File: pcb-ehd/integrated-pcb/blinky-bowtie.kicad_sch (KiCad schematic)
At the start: 93 parts, among them J1 USB_C_Receptacle_USB2.0, J2 JST_PH, J3 SWD, Q1 DMP2045U, SW1 B3U, SW2 B3U, SW3 B3U, U1 MCP73831T-2, U2 ATSAMD21G18A-M, U3 AP2112K-3.3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

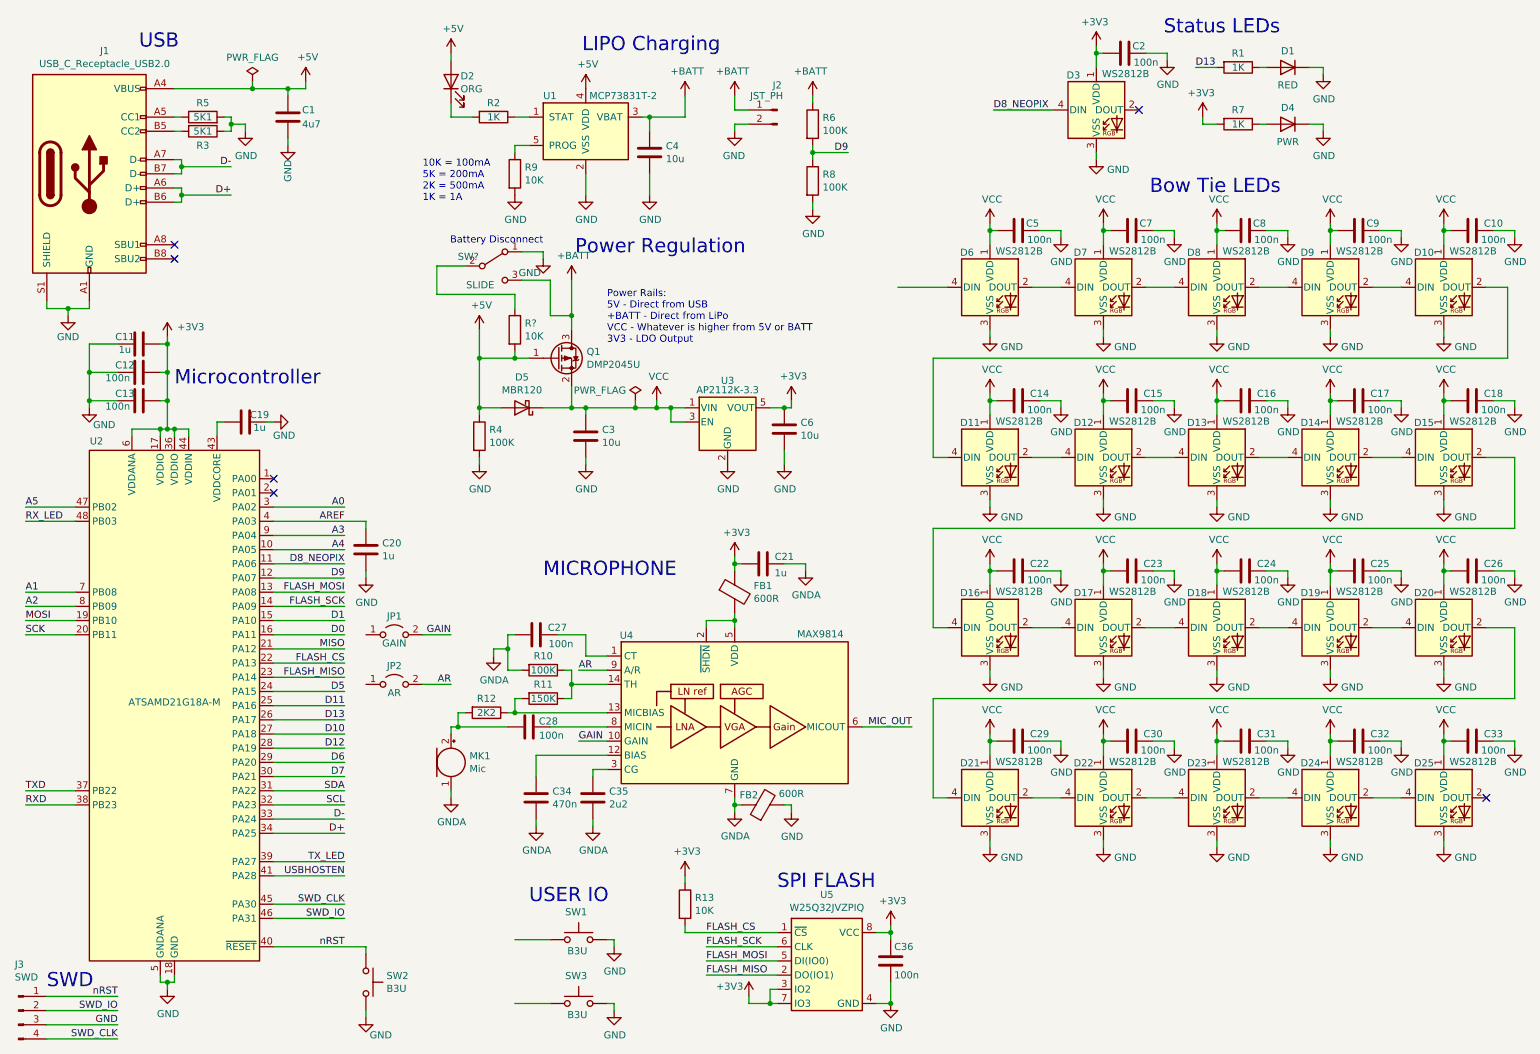
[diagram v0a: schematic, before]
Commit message: bow tie graphics done
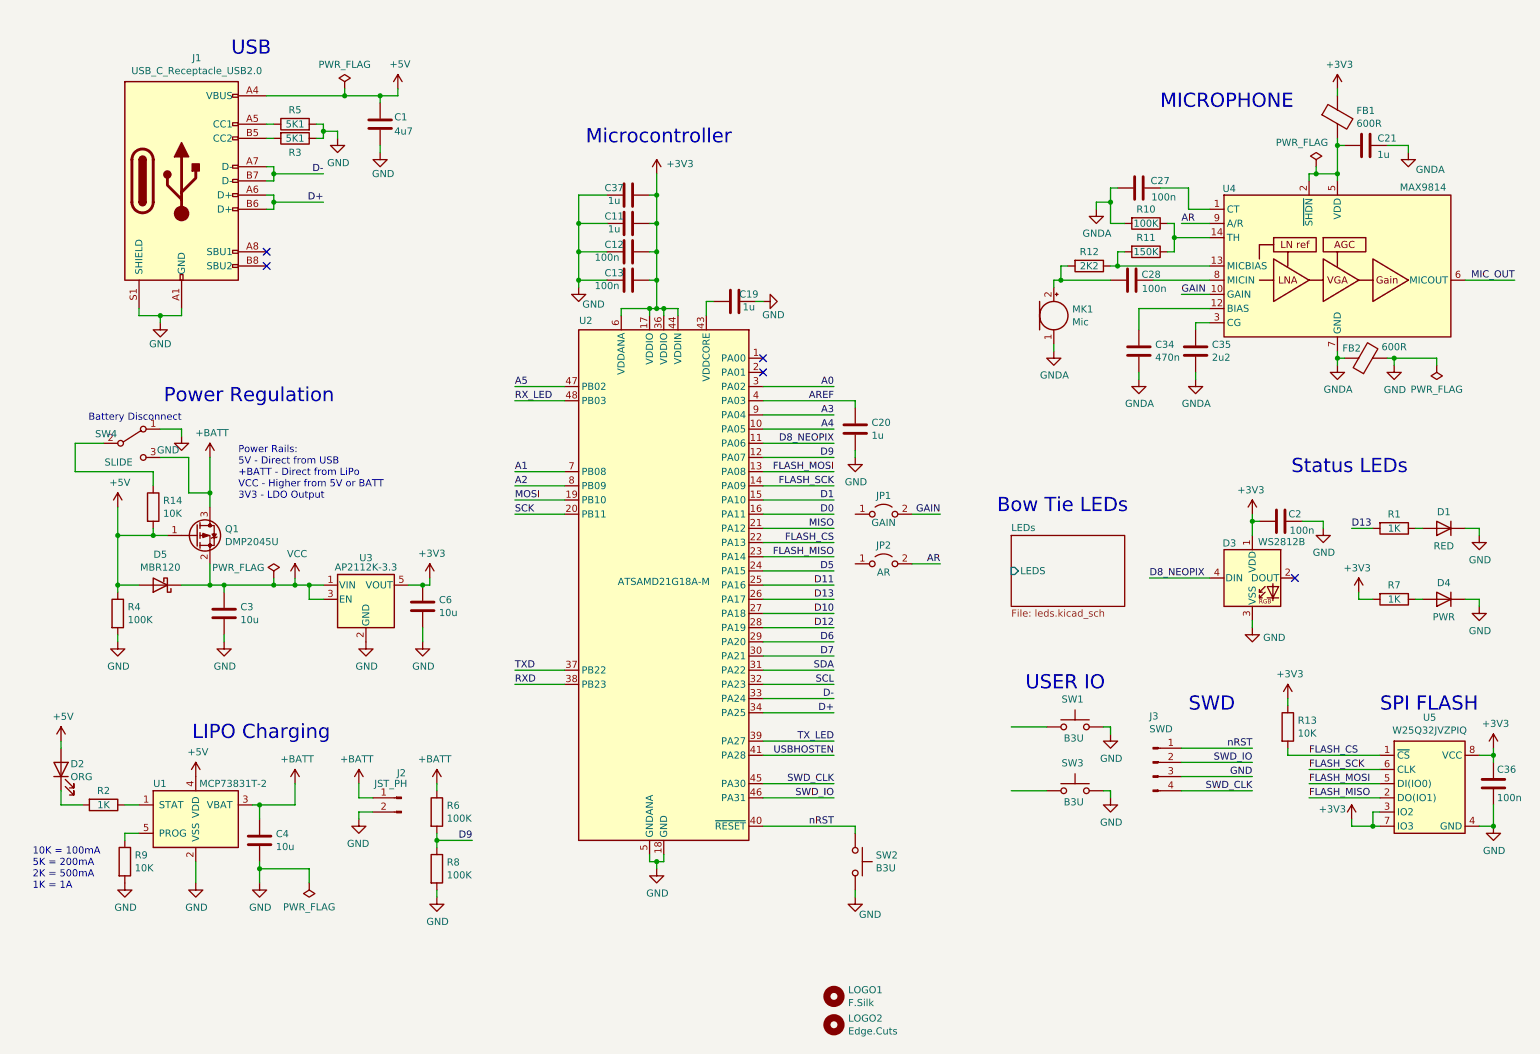
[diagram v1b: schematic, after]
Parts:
- removed C10, C14, C15, C16, C17, C18, C22, C23, C24, C25, C26, C29, C30, C31, C32, C33, C5, C7, C8, C9: 100n, Capacitor_SMD:C_0603_1608Metric, symbol Device:C
- removed D10, D11, D12, D13, D14, D15, D16, D17, D18, D19, D20, D21, D22, D23, D24, D25, D6, D7, D8, D9: WS2812B, LED_SMD:LED_WS2812B_PLCC4_5.0x5.0mm_P3.2mm, symbol LED:WS2812B
- added C37: 1u, Capacitor_SMD:C_0603_1608Metric, symbol Device:C
- added LOGO1: F.Silk, ehd:bowtie-f-silk, symbol Mechanical:MountingHole
- added LOGO2: Edge.Cuts, ehd:bowtie-edge-cuts, symbol Mechanical:MountingHole
- SW4: renamed from SW?; footprint (none) -> ehd:SW_SPDT_PCM12
- gave numbers to parts that had none: 1
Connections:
- net +3V3: now also C37.1; no longer C21.1
- net GND: now also C37.2
- net at FB1.2, U4.2 (~SHDN), U4.5 (VDD): now also C21.1
- no-connect marks 6 -> 5
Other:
- added sheet LEDs (leds.kicad_sch)
- note added: "Power Rails: 5V - Direct from USB +BATT - Direct from LiPo VCC - Higher from 5V or BATT 3V3 - LDO Output"
- note removed: "Power Rails: 5V - Direct from USB +BATT - Direct from LiPo VCC - Whatever is higher from 5V or BATT 3V3 - LDO Output"
- moved on the sheet: C1, C11, C12, C13, C19, C2, C20, C21, C27, C28, C3, C34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

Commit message: rough placement of all but analog
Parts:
- D3: footprint LED_SMD:LED_WS2812B_PLCC4_5.0x5.0mm_P3.2mm -> ehd:LED_WS2812B_PLCC4_5.0x5.0mm_P3.2mm
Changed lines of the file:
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@@
       (effects (font (size 1.27 1.27)) (justify left))
     )
-    (property "Footprint" "LED_SMD:LED_WS2812B_PLCC4_5.0x5.0mm_P3.2mm" (id 2) (at 236.22 121.92 0)
+    (property "Footprint" "ehd:LED_WS2812B_PLCC4_5.0x5.0mm_P3.2mm" (id 2) (at 236.22 121.92 0)
       (effects (font (size 1.27 1.27)) (justify left top) hide)
     )
@@
     )
     (path "/7fb69442-52e3-4c1a-9bf4-99a4ba0d16ef"
-      (reference "D3") (unit 1) (value "WS2812B") (footprint "LED_SMD:LED_WS2812B_PLCC4_5.0x5.0mm_P3.2mm")
+      (reference "D3") (unit 1) (value "WS2812B") (footprint "ehd:LED_WS2812B_PLCC4_5.0x5.0mm_P3.2mm")
     )
     (path "/3e3ddb51-22ac-4836-b03c-bf28224ba3b4"
@@
       (reference "#PWR0196") (unit 1) (value "GND") (footprint "")
     )
+    (path "/79222c86-a946-4b0f-a90e-aa13cf3bd29e/3489d562-055c-4481-af91-dd3d92d6b69b"
+      (reference "#PWR0197") (unit 1) (value "+3V3") (footprint "")
+    )
     (path "/79222c86-a946-4b0f-a90e-aa13cf3bd29e/6a6f2cb1-836a-4eb7-9560-2c25b1ed34e2"
       (reference "C5") (unit 1) (value "100n") (footprint "Capacitor_SMD:C_0603_1608Metric")
@@
     )
     (path "/79222c86-a946-4b0f-a90e-aa13cf3bd29e/5f738c9c-1639-4e2e-b066-98ac121b7c21"
-      (reference "D6") (unit 1) (value "WS2812B") (footprint "LED_SMD:LED_WS2812B_PLCC4_5.0x5.0mm_P3.2mm")
+      (reference "D6") (unit 1) (value "WS2812B") (footprint "ehd:LED_WS2812B_PLCC4_5.0x5.0mm_P3.2mm")
     )
     (path "/79222c86-a946-4b0f-a90e-aa13cf3bd29e/e2dfe95f-8037-4989-824f-602376c18d4d"
-      (reference "D7") (unit 1) (value "WS2812B") (footprint "LED_SMD:LED_WS2812B_PLCC4_5.0x5.0mm_P3.2mm")
+      (reference "D7") (unit 1) (value "WS2812B") (footprint "ehd:LED_WS2812B_PLCC4_5.0x5.0mm_P3.2mm")
     )
     (path "/79222c86-a946-4b0f-a90e-aa13cf3bd29e/8c5a1746-fcd6-46e3-ac57-3ad73fbefa1b"
-      (reference "D8") (unit 1) (value "WS2812B") (footprint "LED_SMD:LED_WS2812B_PLCC4_5.0x5.0mm_P3.2mm")
+      (reference "D8") (unit 1) (value "WS2812B") (footprint "ehd:LED_WS2812B_PLCC4_5.0x5.0mm_P3.2mm")
     )
     (path "/79222c86-a946-4b0f-a90e-aa13cf3bd29e/67cbd563-2c5a-4216-98dc-b58b4efe643c"
-      (reference "D9") (unit 1) (value "WS2812B") (footprint "LED_SMD:LED_WS2812B_PLCC4_5.0x5.0mm_P3.2mm")
+      (reference "D9") (unit 1) (value "WS2812B") (footprint "ehd:LED_WS2812B_PLCC4_5.0x5.0mm_P3.2mm")
     )
     (path "/79222c86-a946-4b0f-a90e-aa13cf3bd29e/8d48d32a-ada1-437c-a709-ded7909fb42d"
-      (reference "D10") (unit 1) (value "WS2812B") (footprint "LED_SMD:LED_WS2812B_PLCC4_5.0x5.0mm_P3.2mm")
+      (reference "D10") (unit 1) (value "WS2812B") (footprint "ehd:LED_WS2812B_PLCC4_5.0x5.0mm_P3.2mm")
     )
     (path "/79222c86-a946-4b0f-a90e-aa13cf3bd29e/07e336a8-93c4-485a-882a-6e6e4804cb60"
-      (reference "D11") (unit 1) (value "WS2812B") (footprint "LED_SMD:LED_WS2812B_PLCC4_5.0x5.0mm_P3.2mm")
+      (reference "D11") (unit 1) (value "WS2812B") (footprint "ehd:LED_WS2812B_PLCC4_5.0x5.0mm_P3.2mm")
     )
     (path "/79222c86-a946-4b0f-a90e-aa13cf3bd29e/154256d0-f08b-4c94-ba46-bed865644c5d"
-      (reference "D12") (unit 1) (value "WS2812B") (footprint "LED_SMD:LED_WS2812B_PLCC4_5.0x5.0mm_P3.2mm")
+      (reference "D12") (unit 1) (value "WS2812B") (footprint "ehd:LED_WS2812B_PLCC4_5.0x5.0mm_P3.2mm")
     )
     (path "/79222c86-a946-4b0f-a90e-aa13cf3bd29e/58c6147d-3656-4ff5-9021-82f135dc3d52"
-      (reference "D13") (unit 1) (value "WS2812B") (footprint "LED_SMD:LED_WS2812B_PLCC4_5.0x5.0mm_P3.2mm")
+      (reference "D13") (unit 1) (value "WS2812B") (footprint "ehd:LED_WS2812B_PLCC4_5.0x5.0mm_P3.2mm")
     )
     (path "/79222c86-a946-4b0f-a90e-aa13cf3bd29e/b05f62fd-53d2-474a-9ad8-1c238a22f93c"
-      (reference "D14") (unit 1) (value "WS2812B") (footprint "LED_SMD:LED_WS2812B_PLCC4_5.0x5.0mm_P3.2mm")
+      (reference "D14") (unit 1) (value "WS2812B") (footprint "ehd:LED_WS2812B_PLCC4_5.0x5.0mm_P3.2mm")
     )
     (path "/79222c86-a946-4b0f-a90e-aa13cf3bd29e/6b39f67f-2ca6-42fb-b929-dc3bc9d5f954"
-      (reference "D15") (unit 1) (value "WS2812B") (footprint "LED_SMD:LED_WS2812B_PLCC4_5.0x5.0mm_P3.2mm")
+      (reference "D15") (unit 1) (value "WS2812B") (footprint "ehd:LED_WS2812B_PLCC4_5.0x5.0mm_P3.2mm")
     )
     (path "/79222c86-a946-4b0f-a90e-aa13cf3bd29e/de2b556c-18c7-4fbd-b35a-3efe53a8651c"
-      (reference "D16") (unit 1) (value "WS2812B") (footprint "LED_SMD:LED_WS2812B_PLCC4_5.0x5.0mm_P3.2mm")
+      (reference "D16") (unit 1) (value "WS2812B") (footprint "ehd:LED_WS2812B_PLCC4_5.0x5.0mm_P3.2mm")
     )
     (path "/79222c86-a946-4b0f-a90e-aa13cf3bd29e/80300823-ece2-4bcc-ae54-c63fa090e136"
-      (reference "D17") (unit 1) (value "WS2812B") (footprint "LED_SMD:LED_WS2812B_PLCC4_5.0x5.0mm_P3.2mm")
+      (reference "D17") (unit 1) (value "WS2812B") (footprint "ehd:LED_WS2812B_PLCC4_5.0x5.0mm_P3.2mm")
     )
     (path "/79222c86-a946-4b0f-a90e-aa13cf3bd29e/79c6e6b0-f4e4-4486-b789-5661387ba461"
-      (reference "D18") (unit 1) (value "WS2812B") (footprint "LED_SMD:LED_WS2812B_PLCC4_5.0x5.0mm_P3.2mm")
+      (reference "D18") (unit 1) (value "WS2812B") (footprint "ehd:LED_WS2812B_PLCC4_5.0x5.0mm_P3.2mm")
     )
     (path "/79222c86-a946-4b0f-a90e-aa13cf3bd29e/5a9d3c1b-0a54-4ec7-b2cf-eb0079784320"
-      (reference "D19") (unit 1) (value "WS2812B") (footprint "LED_SMD:LED_WS2812B_PLCC4_5.0x5.0mm_P3.2mm")
+      (reference "D19") (unit 1) (value "WS2812B") (footprint "ehd:LED_WS2812B_PLCC4_5.0x5.0mm_P3.2mm")
     )
     (path "/79222c86-a946-4b0f-a90e-aa13cf3bd29e/190f07e5-9d6c-4ddb-a657-5bc9ca51fed0"
-      (reference "D20") (unit 1) (value "WS2812B") (footprint "LED_SMD:LED_WS2812B_PLCC4_5.0x5.0mm_P3.2mm")
+      (reference "D20") (unit 1) (value "WS2812B") (footprint "ehd:LED_WS2812B_PLCC4_5.0x5.0mm_P3.2mm")
     )
     (path "/79222c86-a946-4b0f-a90e-aa13cf3bd29e/022b41ed-01de-4a67-b9f4-899efbd6736f"
-      (reference "D21") (unit 1) (value "WS2812B") (footprint "LED_SMD:LED_WS2812B_PLCC4_5.0x5.0mm_P3.2mm")
+      (reference "D21") (unit 1) (value "WS2812B") (footprint "ehd:LED_WS2812B_PLCC4_5.0x5.0mm_P3.2mm")
     )
     (path "/79222c86-a946-4b0f-a90e-aa13cf3bd29e/a300473a-124f-4f35-8cbb-733e46919c56"
-      (reference "D22") (unit 1) (value "WS2812B") (footprint "LED_SMD:LED_WS2812B_PLCC4_5.0x5.0mm_P3.2mm")
+      (reference "D22") (unit 1) (value "WS2812B") (footprint "ehd:LED_WS2812B_PLCC4_5.0x5.0mm_P3.2mm")
     )
     (path "/79222c86-a946-4b0f-a90e-aa13cf3bd29e/5f29541c-157c-45f7-9b90-7c7ab31cae56"
-      (reference "D23") (unit 1) (value "WS2812B") (footprint "LED_SMD:LED_WS2812B_PLCC4_5.0x5.0mm_P3.2mm")
+      (reference "D23") (unit 1) (value "WS2812B") (footprint "ehd:LED_WS2812B_PLCC4_5.0x5.0mm_P3.2mm")
     )
     (path "/79222c86-a946-4b0f-a90e-aa13cf3bd29e/d545a5a1-8325-476c-a3f1-169c17007c4e"
-      (reference "D24") (unit 1) (value "WS2812B") (footprint "LED_SMD:LED_WS2812B_PLCC4_5.0x5.0mm_P3.2mm")
+      (reference "D24") (unit 1) (value "WS2812B") (footprint "ehd:LED_WS2812B_PLCC4_5.0x5.0mm_P3.2mm")
     )
     (path "/79222c86-a946-4b0f-a90e-aa13cf3bd29e/7aa666b3-8e0c-4a54-a304-c2c4b2ef497c"
-      (reference "D25") (unit 1) (value "WS2812B") (footprint "LED_SMD:LED_WS2812B_PLCC4_5.0x5.0mm_P3.2mm")
+      (reference "D25") (unit 1) (value "WS2812B") (footprint "ehd:LED_WS2812B_PLCC4_5.0x5.0mm_P3.2mm")
     )
     (path "/79222c86-a946-4b0f-a90e-aa13cf3bd29e/b0fc9718-f9a5-4e23-8f4e-47696537b0c2"

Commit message: layout passes DRC
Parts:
- added H1, H2, H3, H4: M2, MountingHole:MountingHole_2.2mm_M2_DIN965, symbol Mechanical:MountingHole
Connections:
- net A0: now also JP1.1 (A)
- net A2: now also JP2.1 (A)
- net D1: now also SW1.1
- net SCK: now also SW3.1
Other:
- note added: "Slide = HIGH Disconnected"
- moved on the sheet: JP1, JP2
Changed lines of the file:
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@@
     (stroke (width 0) (type solid) (color 0 0 0 0))
   )
+  (wire (pts (xy 87.63 97.79) (xy 92.71 97.79))
+    (stroke (width 0) (type solid) (color 0 0 0 0))
+  )
   (wire (pts (xy 87.63 115.57) (xy 87.63 114.3))
     (stroke (width 0) (type solid) (color 0 0 0 0))
@@
     (stroke (width 0) (type solid) (color 0 0 0 0))
   )
-  (wire (pts (xy 179.07 102.87) (xy 173.99 102.87))
+  (wire (pts (xy 175.26 80.01) (xy 170.18 80.01))
     (stroke (width 0) (type solid) (color 0 0 0 0))
   )
-  (wire (pts (xy 179.07 111.76) (xy 173.99 111.76))
+  (wire (pts (xy 180.34 113.03) (xy 191.77 113.03))
     (stroke (width 0) (type solid) (color 0 0 0 0))
   )
@@
     (effects (font (size 1.27 1.27)) (justify left bottom))
   )
+  (text "Slide = HIGH\nDisconnected" (at 29.21 101.6 180)
+    (effects (font (size 1.27 1.27)) (justify right bottom))
+  )
   (text "Power Regulation" (at 40.005 83.185 0)
     (effects (font (size 2.54 2.54)) (justify left bottom))
@@
     (effects (font (size 1.27 1.27)) (justify right bottom))
   )
+  (label "AR" (at 87.63 97.79 0)
+    (effects (font (size 1.27 1.27)) (justify left bottom))
+  )
   (label "D9" (at 95.25 161.29 180)
     (effects (font (size 1.27 1.27)) (justify right bottom))
@@
     (effects (font (size 1.27 1.27)) (justify right bottom))
   )
-  (label "GAIN" (at 179.07 102.87 180)
+  (label "GAIN" (at 175.26 80.01 180)
     (effects (font (size 1.27 1.27)) (justify right bottom))
   )
-  (label "AR" (at 179.07 111.76 180)
-    (effects (font (size 1.27 1.27)) (justify right bottom))
+  (label "D5" (at 180.34 113.03 0)
+    (effects (font (size 1.27 1.27)) (justify left bottom))
+  )
+  (label "D1" (at 191.77 140.97 0)
+    (effects (font (size 1.27 1.27)) (justify left bottom))
+  )
+  (label "SCK" (at 191.77 152.4 0)
+    (effects (font (size 1.27 1.27)) (justify left bottom))
   )
   (label "D8_NEOPIX" (at 216.535 114.3 0)
@@
     (pin "1")
   )
+  (symbol (lib_id "Mechanical:MountingHole") (at 133.35 189.23 0) (unit 1)
+    (in_bom yes) (on_board yes)
+    (property "Reference" "H1" (id 0) (at 135.8901 188.0806 0)
+      (effects (font (size 1.27 1.27)) (justify left))
+    )
+    (property "Value" "M2" (id 1) (at 135.89 190.379 0)
+      (effects (font (size 1.27 1.27)) (justify left))
+    )
+    (property "Footprint" "MountingHole:MountingHole_2.2mm_M2_DIN965" (id 2) (at 133.35 189.23 0)
+      (effects (font (size 1.27 1.27)) hide)
+    )
+    (property "Datasheet" "~" (id 3) (at 133.35 189.23 0)
+      (effects (font (size 1.27 1.27)) hide)
+    )
+  )
+  (symbol (lib_id "Mechanical:MountingHole") (at 133.35 194.31 0) (unit 1)
+    (in_bom yes) (on_board yes)
+    (property "Reference" "H3" (id 0) (at 135.8901 193.1606 0)
+      (effects (font (size 1.27 1.27)) (justify left))
+    )
+    (property "Value" "M2" (id 1) (at 135.89 195.459 0)
+      (effects (font (size 1.27 1.27)) (justify left))
+    )
+    (property "Footprint" "MountingHole:MountingHole_2.2mm_M2_DIN965" (id 2) (at 133.35 194.31 0)
+      (effects (font (size 1.27 1.27)) hide)
+    )
+    (property "Datasheet" "~" (id 3) (at 133.35 194.31 0)
+      (effects (font (size 1.27 1.27)) hide)
+    )
+  )
+  (symbol (lib_id "Mechanical:MountingHole") (at 140.97 189.23 0) (unit 1)
+    (in_bom yes) (on_board yes)
+    (property "Reference" "H2" (id 0) (at 143.5101 188.0806 0)
+      (effects (font (size 1.27 1.27)) (justify left))
+    )
+    (property "Value" "M2" (id 1) (at 143.51 190.379 0)
+      (effects (font (size 1.27 1.27)) (justify left))
+    )
+    (property "Footprint" "MountingHole:MountingHole_2.2mm_M2_DIN965" (id 2) (at 140.97 189.23 0)
+      (effects (font (size 1.27 1.27)) hide)
+    )
+    (property "Datasheet" "~" (id 3) (at 140.97 189.23 0)
+      (effects (font (size 1.27 1.27)) hide)
+    )
+  )
+  (symbol (lib_id "Mechanical:MountingHole") (at 140.97 194.31 0) (unit 1)
+    (in_bom yes) (on_board yes)
+    (property "Reference" "H4" (id 0) (at 143.5101 193.1606 0)
+      (effects (font (size 1.27 1.27)) (justify left))
+    )
+    (property "Value" "M2" (id 1) (at 143.51 195.459 0)
+      (effects (font (size 1.27 1.27)) (justify left))
+    )
+    (property "Footprint" "MountingHole:MountingHole_2.2mm_M2_DIN965" (id 2) (at 140.97 194.31 0)
+      (effects (font (size 1.27 1.27)) hide)
+    )
+    (property "Datasheet" "~" (id 3) (at 140.97 194.31 0)
+      (effects (font (size 1.27 1.27)) hide)
+    )
+  )
   (symbol (lib_id "Mechanical:MountingHole") (at 160.02 189.23 0) (unit 1)
     (in_bom no) (on_board yes)
@@
     (pin "2")
   )
-  (symbol (lib_id "Jumper:Jumper_2_Open") (at 168.91 102.87 0) (unit 1)
+  (symbol (lib_id "Jumper:Jumper_2_Open") (at 97.79 97.79 0) (mirror y) (unit 1)
     (in_bom yes) (on_board yes)
-    (property "Reference" "JP1" (id 0) (at 168.91 99.5488 0))
-    (property "Value" "GAIN" (id 1) (at 168.91 104.388 0))
-    (property "Footprint" "Jumper:SolderJumper-2_P1.3mm_Bridged_RoundedPad1.0x1.5mm" (id 2) (at 168.91 102.87 0)
+    (property "Reference" "JP2" (id 0) (at 97.79 94.4688 0))
+    (property "Value" "AR" (id 1) (at 97.79 99.307 0))
+    (property "Footprint" "Jumper:SolderJumper-2_P1.3mm_Bridged_RoundedPad1.0x1.5mm" (id 2) (at 97.79 97.79 0)
       (effects (font (size 1.27 1.27)) hide)
     )
-    (property "Datasheet" "~" (id 3) (at 168.91 102.87 0)
+    (property "Datasheet" "~" (id 3) (at 97.79 97.79 0)
       (effects (font (size 1.27 1.27)) hide)
     )
@@
     (pin "2")
   )
-  (symbol (lib_id "Jumper:Jumper_2_Open") (at 168.91 111.76 0) (unit 1)
+  (symbol (lib_id "Jumper:Jumper_2_Open") (at 165.1 80.01 0) (unit 1)
     (in_bom yes) (on_board yes)
-    (property "Reference" "JP2" (id 0) (at 168.91 108.4388 0))
-    (property "Value" "AR" (id 1) (at 168.91 113.277 0))
-    (property "Footprint" "Jumper:SolderJumper-2_P1.3mm_Bridged_RoundedPad1.0x1.5mm" (id 2) (at 168.91 111.76 0)
+    (property "Reference" "JP1" (id 0) (at 165.1 76.6888 0))
+    (property "Value" "GAIN" (id 1) (at 165.1 81.528 0))
+    (property "Footprint" "Jumper:SolderJumper-2_P1.3mm_Bridged_RoundedPad1.0x1.5mm" (id 2) (at 165.1 80.01 0)
       (effects (font (size 1.27 1.27)) hide)
     )
-    (property "Datasheet" "~" (id 3) (at 168.91 111.76 0)
+    (property "Datasheet" "~" (id 3) (at 165.1 80.01 0)
       (effects (font (size 1.27 1.27)) hide)
     )
@@
       (reference "FB2") (unit 1) (value "600R") (footprint "Resistor_SMD:R_0603_1608Metric")
     )
+    (path "/a6eea884-4909-4743-b493-f463d9436595"
+      (reference "H1") (unit 1) (value "M2") (footprint "MountingHole:MountingHole_2.2mm_M2_DIN965")
+    )
+    (path "/84770d33-de74-49be-bc80-be7b235ba24b"
+      (reference "H2") (unit 1) (value "M2") (footprint "MountingHole:MountingHole_2.2mm_M2_DIN965")
+    )
+    (path "/26813fc0-e72c-4ae4-8357-662e3566ac85"
+      (reference "H3") (unit 1) (value "M2") (footprint "MountingHole:MountingHole_2.2mm_M2_DIN965")
+    )
+    (path "/2385c06a-6ef8-469c-8763-7881e879bafb"
+      (reference "H4") (unit 1) (value "M2") (footprint "MountingHole:MountingHole_2.2mm_M2_DIN965")
+    )
     (path "/00000000-0000-0000-0000-00005ff3338b"
